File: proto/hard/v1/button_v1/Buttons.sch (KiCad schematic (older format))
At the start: 38 parts, among them J1 Conn_01x06_Female, J2 Conn_01x06_Female, J3 Conn_01x06_Female, J4 Conn_01x06_Female, Q10 Q_NPN_BEC, Q11 Q_NPN_BEC, Q12 Q_NPN_BEC, Q13 Q_NPN_BEC, Q6 UMG8N, Q7 UMG8N, U13 74HC595, U6 LM339

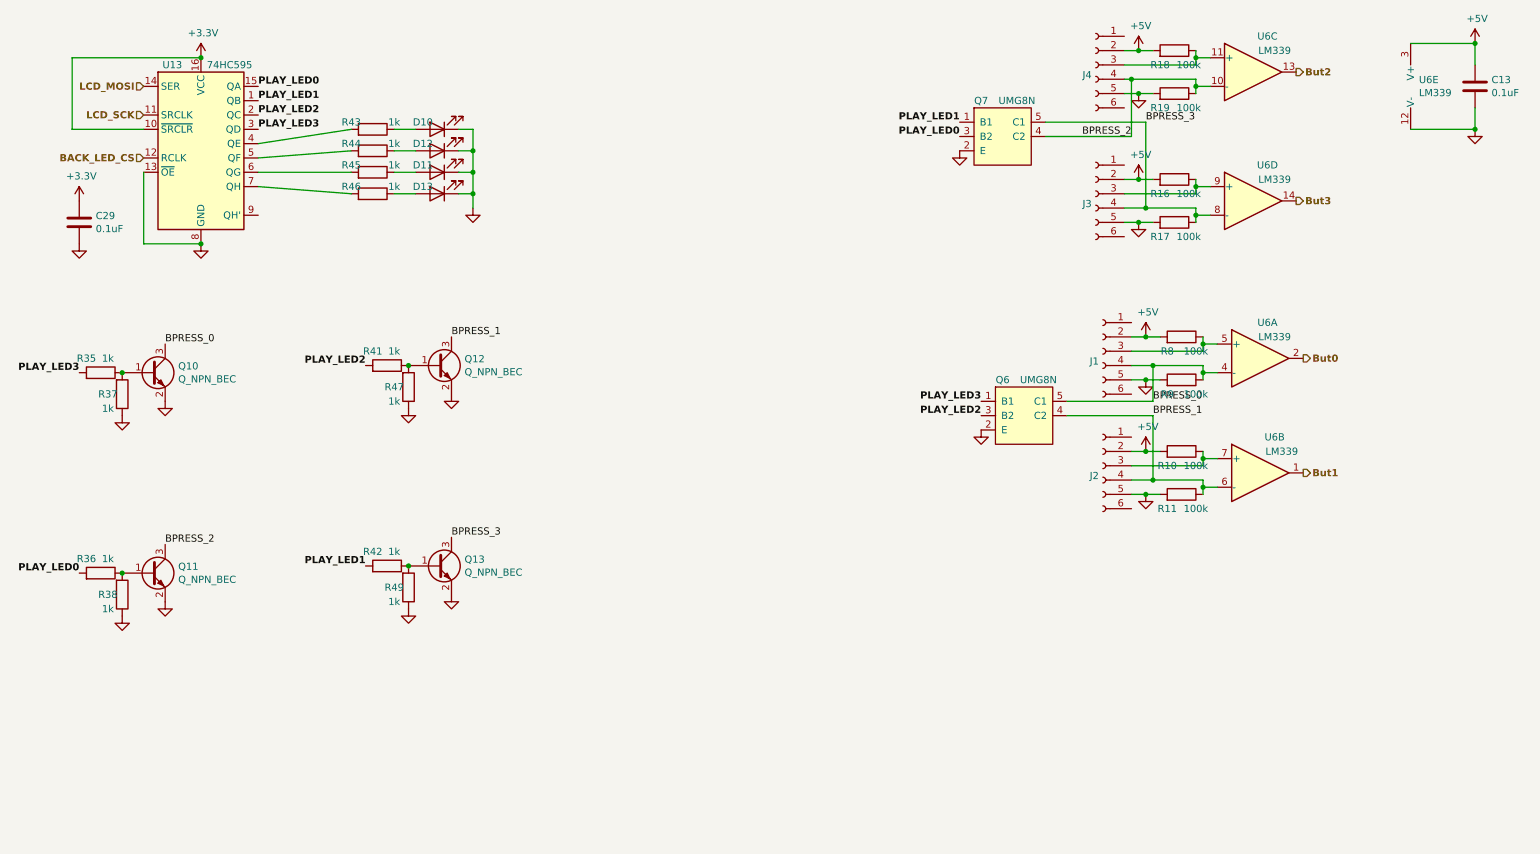
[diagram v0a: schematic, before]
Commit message: BOOT0 connected to GND Due to migration to Kicad V5.1.6 had to change text style from "bold" to "normal"
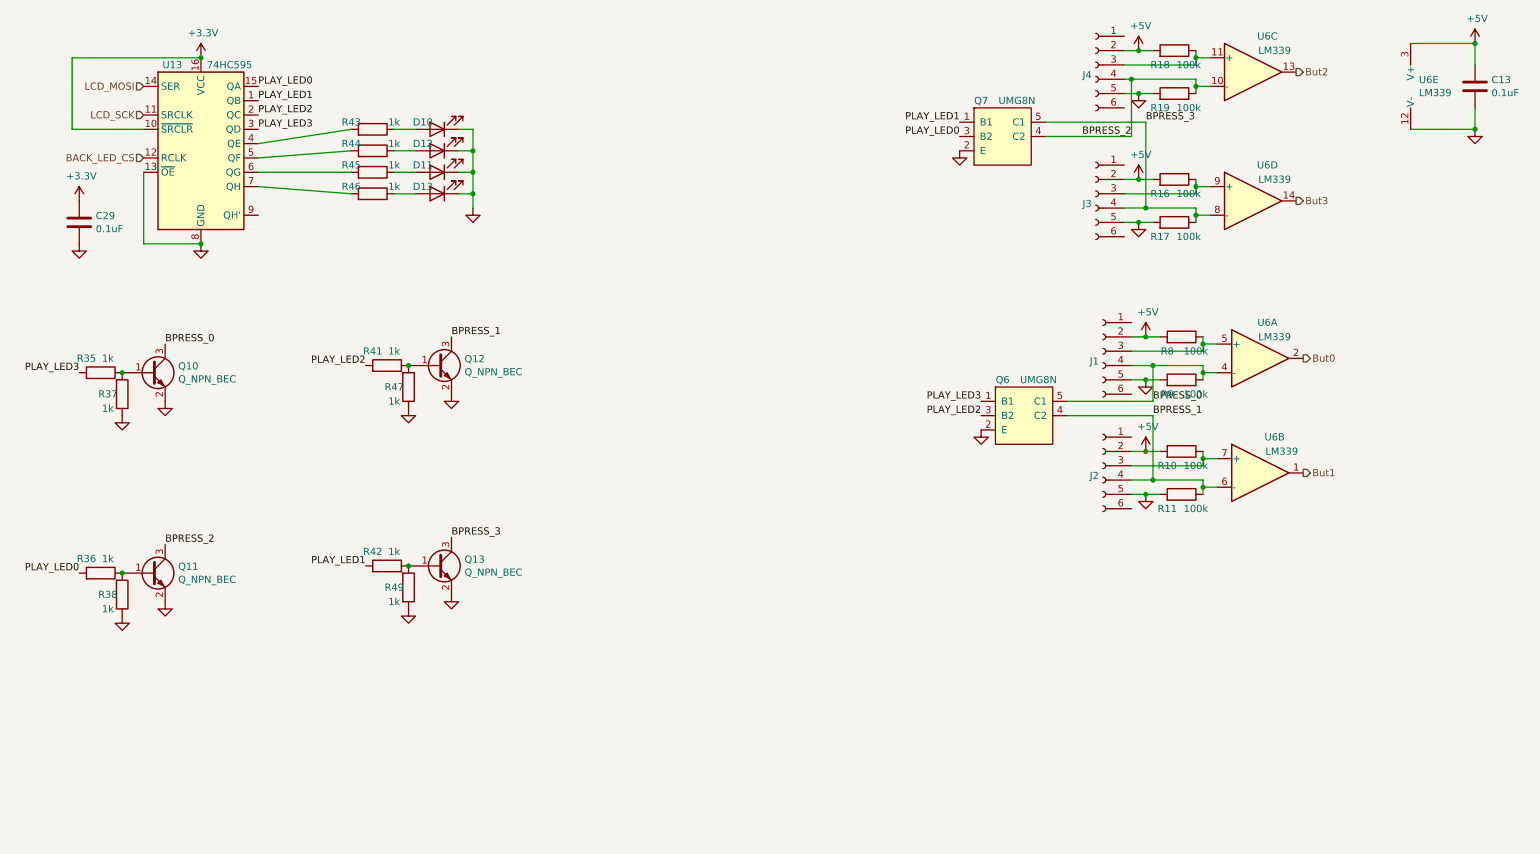
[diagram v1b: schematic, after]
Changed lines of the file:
@@
 EESchema Schematic File Version 4
-LIBS:button_v1-cache
-EELAYER 29 0
+EELAYER 30 0
 EELAYER END
 $Descr A4 11693 8268
@@
 Comment4 ""
 $EndDescr
-Text HLabel 1500 1200 0    50   Input ~ 6
+Text HLabel 1500 1200 0    50   Input ~ 0
 LCD_MOSI
-Text HLabel 1500 1400 0    50   Input ~ 6
+Text HLabel 1500 1400 0    50   Input ~ 0
 LCD_SCK
-Text HLabel 1500 1700 0    50   Input ~ 6
+Text HLabel 1500 1700 0    50   Input ~ 0
 BACK_LED_CS
-Text HLabel 9600 3100 2    50   Output ~ 6
+Text HLabel 9600 3100 2    50   Output ~ 0
 But0
-Text HLabel 9600 3900 2    50   Output ~ 6
+Text HLabel 9600 3900 2    50   Output ~ 0
 But1
-Text HLabel 9550 1100 2    50   Output ~ 6
+Text HLabel 9550 1100 2    50   Output ~ 0
 But2
-Text HLabel 9550 2000 2    50   Output ~ 6
+Text HLabel 9550 2000 2    50   Output ~ 0
 But3
 $Comp
@@
 	1000 1000 1900 1000
 Connection ~ 1900 1000
-Text Label 2300 1200 0    50   ~ 6
+Text Label 2300 1200 0    50   ~ 0
 PLAY_LED0
-Text Label 2300 1300 0    50   ~ 6
+Text Label 2300 1300 0    50   ~ 0
 PLAY_LED1
-Text Label 2300 1400 0    50   ~ 6
+Text Label 2300 1400 0    50   ~ 0
 PLAY_LED2
-Text Label 2300 1500 0    50   ~ 6
+Text Label 2300 1500 0    50   ~ 0
 PLAY_LED3
 $Comp
@@
 Wire Wire Line
 	7950 3400 8550 3400
-Text Label 7200 1550 2    50   ~ 6
+Text Label 7200 1550 2    50   ~ 0
 PLAY_LED0
-Text Label 7200 1450 2    50   ~ 6
+Text Label 7200 1450 2    50   ~ 0
 PLAY_LED1
-Text Label 7350 3500 2    50   ~ 6
+Text Label 7350 3500 2    50   ~ 0
 PLAY_LED2
-Text Label 7350 3400 2    50   ~ 6
+Text Label 7350 3400 2    50   ~ 0
 PLAY_LED3
 Wire Wire Line
@@
 	1    0    0    -1
 $EndComp
-Text Label 3050 3150 2    50   ~ 6
+Text Label 3050 3150 2    50   ~ 0
 PLAY_LED2
-Text Label 1050 3200 2    50   ~ 6
+Text Label 1050 3200 2    50   ~ 0
 PLAY_LED3
-Text Label 3050 4550 2    50   ~ 6
+Text Label 3050 4550 2    50   ~ 0
 PLAY_LED1
-Text Label 1050 4600 2    50   ~ 6
+Text Label 1050 4600 2    50   ~ 0
 PLAY_LED0
 $EndSCHEMATC

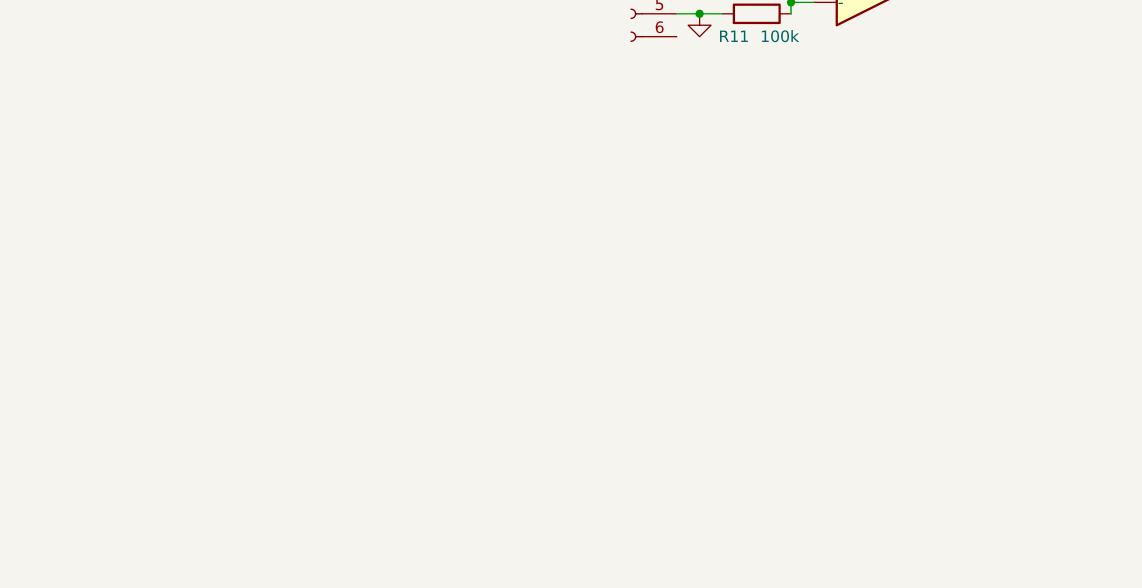
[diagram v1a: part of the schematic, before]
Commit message: Rework of main board prototype. Work not finished.
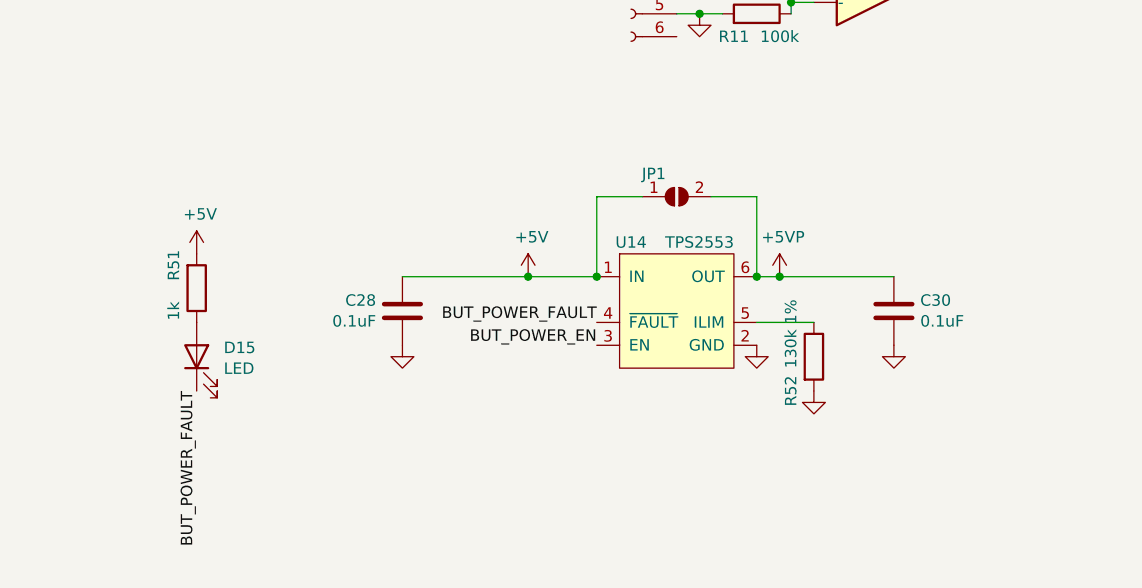
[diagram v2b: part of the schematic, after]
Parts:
- added C28, C30: 0.1uF, Capacitor_SMD:C_0805_2012Metric_Pad1.15x1.40mm_HandSolder, symbol Device:C
- added D15: LED, LED_THT:LED_D3.0mm, symbol Device:LED
- added JP1: SolderJumper_2_Open, Jumper:SolderJumper-2_P1.3mm_Open_TrianglePad1.0x1.5mm, symbol Jumper:SolderJumper_2_Open
- added R51: 1k, Resistor_SMD:R_0805_2012Metric_Pad1.15x1.40mm_HandSolder, symbol Device:R
- added R52: 130k 1%, Resistor_SMD:R_0805_2012Metric_Pad1.15x1.40mm_HandSolder, symbol Device:R
- added U14: TPS2553, Package_TO_SOT_SMD:SOT-23-6, symbol brbuttonsystem:TPS2553
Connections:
- net +5V: now also C28.1, JP1.1 (A), R51.2, U14.1 (IN)
- net GND: now also C28.2, C30.2, R52.2, U14.2 (GND)
- new net: R52.1, U14.5 (ILIM)
- new net: D15.2 (A), R51.1
- new net +5VP: C30.1, JP1.2 (B), U14.6 (OUT)
- new net BUT_POWER_EN: U14.3 (EN)
- new net BUT_POWER_FAULT: D15.1 (K), U14.4 (~FAULT)
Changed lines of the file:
@@
 Text Label 1050 4600 2    50   ~ 0
 PLAY_LED0
+$Comp
+L power:+5VP #PWR0172
+U 1 1 5F37C230
+P 8850 5200
+F 0 "#PWR0172" H 8850 5050 50  0001 C CNN
+F 1 "+5VP" H 8865 5373 50  0000 C CNN
+F 2 "" H 8850 5200 50  0001 C CNN
+F 3 "" H 8850 5200 50  0001 C CNN
+	1    8850 5200
+	1    0    0    -1
+$EndComp
+$Comp
+L Device:C C?
+U 1 1 5F37D386
+P 9350 5350
+AR Path="/5F37D386" Ref="C?"  Part="1"
+AR Path="/5ECDBE8F/5F37D386" Ref="C30"  Part="1"
+F 0 "C30" H 9465 5396 50  0000 L CNN
+F 1 "0.1uF" H 9465 5305 50  0000 L CNN
+F 2 "Capacitor_SMD:C_0805_2012Metric_Pad1.15x1.40mm_HandSolder" H 9388 5200 50  0001 C CNN
+F 3 "~" H 9350 5350 50  0001 C CNN
+	1    9350 5350
+	1    0    0    -1
+$EndComp
+$Comp
+L Device:C C?
+U 1 1 5F37DB14
+P 7200 5350
+AR Path="/5F37DB14" Ref="C?"  Part="1"
+AR Path="/5ECDBE8F/5F37DB14" Ref="C28"  Part="1"
+F 0 "C28" H 7315 5396 50  0000 L CNN
+F 1 "0.1uF" H 7315 5305 50  0000 L CNN
+F 2 "Capacitor_SMD:C_0805_2012Metric_Pad1.15x1.40mm_HandSolder" H 7238 5200 50  0001 C CNN
+F 3 "~" H 7200 5350 50  0001 C CNN
+	1    7200 5350
+	-1   0    0    -1
+$EndComp
+$Comp
+L power:GND #PWR?
+U 1 1 5F384B69
+P 9000 5700
+AR Path="/5F384B69" Ref="#PWR?"  Part="1"
+AR Path="/5ECDBE8F/5F384B69" Ref="#PWR0173"  Part="1"
+F 0 "#PWR0173" H 9000 5450 50  0001 C CNN
+F 1 "GND" H 9005 5527 50  0001 C CNN
+F 2 "" H 9000 5700 50  0001 C CNN
+F 3 "" H 9000 5700 50  0001 C CNN
+	1    9000 5700
+	1    0    0    -1
+$EndComp
+Wire Wire Line
+	9350 5200 8850 5200
+Connection ~ 8850 5200
+Wire Wire Line
+	8850 5200 8750 5200
+$Comp
+L Device:R R?
+U 1 1 5F38AB1A
+P 9000 5550
+AR Path="/5F38AB1A" Ref="R?"  Part="1"
+AR Path="/5ECDBE8F/5F38AB1A" Ref="R52"  Part="1"
+F 0 "R52" V 8900 5400 50  0000 C CNN
+F 1 "130k 1%" V 8900 5650 50  0000 C CNN
+F 2 "Resistor_SMD:R_0805_2012Metric_Pad1.15x1.40mm_HandSolder" V 8930 5550 50  0001 C CNN
+F 3 "~" H 9000 5550 50  0001 C CNN
+	1    9000 5550
+	1    0    0    -1
+$EndComp
+$Comp
+L power:GND #PWR?
+U 1 1 5F38E54D
+P 8750 5500
+AR Path="/5F38E54D" Ref="#PWR?"  Part="1"
+AR Path="/5ECDBE8F/5F38E54D" Ref="#PWR0174"  Part="1"
+F 0 "#PWR0174" H 8750 5250 50  0001 C CNN
+F 1 "GND" H 8755 5327 50  0001 C CNN
+F 2 "" H 8750 5500 50  0001 C CNN
+F 3 "" H 8750 5500 50  0001 C CNN
+	1    8750 5500
+	1    0    0    -1
+$EndComp
+Wire Wire Line
+	9000 5400 8750 5400
+$Comp
+L power:GND #PWR?
+U 1 1 5F396179
+P 9350 5500
+AR Path="/5F396179" Ref="#PWR?"  Part="1"
+AR Path="/5ECDBE8F/5F396179" Ref="#PWR0175"  Part="1"
+F 0 "#PWR0175" H 9350 5250 50  0001 C CNN
+F 1 "GND" H 9355 5327 50  0001 C CNN
+F 2 "" H 9350 5500 50  0001 C CNN
+F 3 "" H 9350 5500 50  0001 C CNN
+	1    9350 5500
+	1    0    0    -1
+$EndComp
+Wire Wire Line
+	8050 5200 7750 5200
+$Comp
+L power:+5V #PWR?
+U 1 1 5F39A401
+P 7750 5200
+AR Path="/5F39A401" Ref="#PWR?"  Part="1"
+AR Path="/5ECDBE8F/5F39A401" Ref="#PWR0176"  Part="1"
+F 0 "#PWR0176" H 7750 5050 50  0001 C CNN
+F 1 "+5V" H 7765 5373 50  0000 C CNN
+F 2 "" H 7750 5200 50  0001 C CNN
+F 3 "" H 7750 5200 50  0001 C CNN
+	1    7750 5200
+	1    0    0    -1
+$EndComp
+Connection ~ 7750 5200
+Wire Wire Line
+	7750 5200 7200 5200
+$Comp
+L power:GND #PWR?
+U 1 1 5F39AA9F
+P 7200 5500
+AR Path="/5F39AA9F" Ref="#PWR?"  Part="1"
+AR Path="/5ECDBE8F/5F39AA9F" Ref="#PWR0177"  Part="1"
+F 0 "#PWR0177" H 7200 5250 50  0001 C CNN
+F 1 "GND" H 7205 5327 50  0001 C CNN
+F 2 "" H 7200 5500 50  0001 C CNN
+F 3 "" H 7200 5500 50  0001 C CNN
+	1    7200 5500
+	1    0    0    -1
+$EndComp
+Text Label 8050 5400 2    50   ~ 0
+BUT_POWER_FAULT
+Text Label 8050 5500 2    50   ~ 0
+BUT_POWER_EN
+Text Label 6300 5700 3    50   ~ 0
+BUT_POWER_FAULT
+$Comp
+L Device:LED D15
+U 1 1 5F39D445
+P 6300 5550
+F 0 "D15" V 6339 5432 50  0000 R CNN
+F 1 "LED" V 6248 5432 50  0000 R CNN
+F 2 "LED_THT:LED_D3.0mm" H 6300 5550 50  0001 C CNN
+F 3 "~" H 6300 5550 50  0001 C CNN
+	1    6300 5550
+	0    -1   -1   0
+$EndComp
+$Comp
+L power:+5V #PWR?
+U 1 1 5F39CAAC
+P 6300 5100
+AR Path="/5F39CAAC" Ref="#PWR?"  Part="1"
+AR Path="/5ECDBE8F/5F39CAAC" Ref="#PWR0178"  Part="1"
+F 0 "#PWR0178" H 6300 4950 50  0001 C CNN
+F 1 "+5V" H 6315 5273 50  0000 C CNN
+F 2 "" H 6300 5100 50  0001 C CNN
+F 3 "" H 6300 5100 50  0001 C CNN
+	1    6300 5100
+	1    0    0    -1
+$EndComp
+$Comp
+L Device:R R?
+U 1 1 5F39B7BF
+P 6300 5250
+AR Path="/5F39B7BF" Ref="R?"  Part="1"
+AR Path="/5ECDBE8F/5F39B7BF" Ref="R51"  Part="1"
+F 0 "R51" V 6200 5150 50  0000 C CNN
+F 1 "1k" V 6200 5350 50  0000 C CNN
+F 2 "Resistor_SMD:R_0805_2012Metric_Pad1.15x1.40mm_HandSolder" V 6230 5250 50  0001 C CNN
+F 3 "~" H 6300 5250 50  0001 C CNN
+	1    6300 5250
+	1    0    0    1
+$EndComp
+$Comp
+L Jumper:SolderJumper_2_Open JP1
+U 1 1 5F3B9B77
+P 8400 4850
+F 0 "JP1" H 8300 4950 50  0000 C CNN
+F 1 "SolderJumper_2_Open" H 8400 4964 50  0001 C CNN
+F 2 "Jumper:SolderJumper-2_P1.3mm_Open_TrianglePad1.0x1.5mm" H 8400 4850 50  0001 C CNN
+F 3 "~" H 8400 4850 50  0001 C CNN
+	1    8400 4850
+	1    0    0    -1
+$EndComp
+Wire Wire Line
+	8250 4850 8050 4850
+Wire Wire Line
+	8050 4850 8050 5200
+Wire Wire Line
+	8550 4850 8750 4850
+Wire Wire Line
+	8750 4850 8750 5200
+$Comp
+L brbuttonsystem:TPS2553 U14
+U 1 1 5F4424B7
+P 8150 5100
+F 0 "U14" H 8200 5150 50  0000 C CNN
+F 1 "TPS2553" H 8500 5150 50  0000 C CNN
+F 2 "Package_TO_SOT_SMD:SOT-23-6" H 8150 5100 50  0001 C CNN
+F 3 "" H 8150 5100 50  0001 C CNN
+	1    8150 5100
+	1    0    0    -1
+$EndComp
+Connection ~ 8050 5200
+Connection ~ 8750 5200
 $EndSCHEMATC
